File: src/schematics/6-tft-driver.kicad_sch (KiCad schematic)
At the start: 31 parts, among them Q601 NX6008NBKW, Q602 BC847BS, Q603 BC847BS, U601 TMUX1574RSV, U602 TMUX1574RSV, U603 TMUX1574RSV

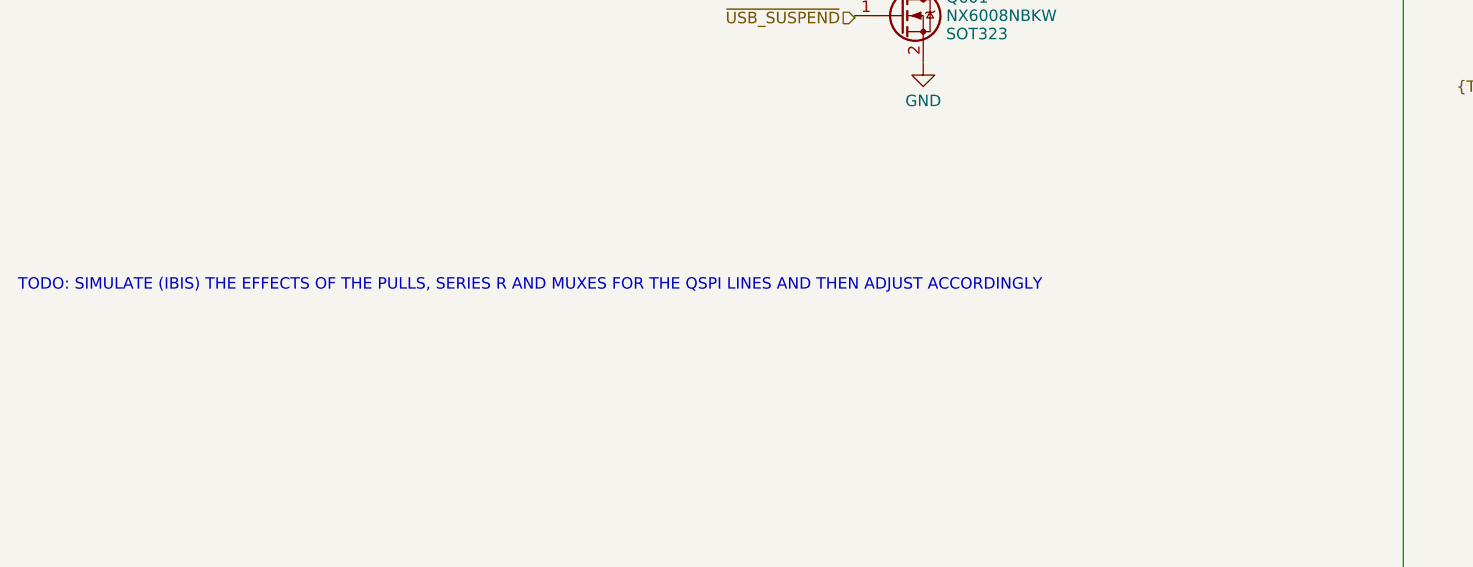
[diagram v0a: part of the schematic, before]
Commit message: Various tidy-ups and checks, mainly around the bypass capacitors.  Added a load of test points.
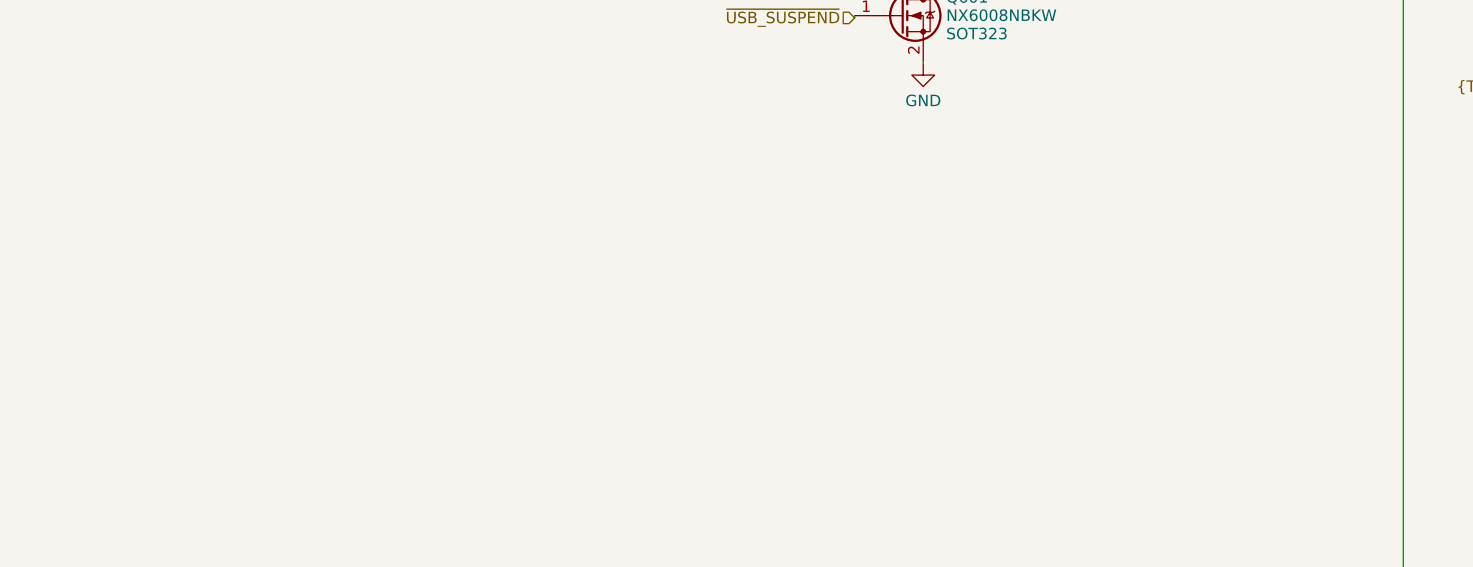
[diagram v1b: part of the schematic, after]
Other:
- note removed: "TODO: SIMULATE (IBIS) THE EFFECTS OF THE PULLS, SERIES R AND MUXES FOR THE QSPI LINES AND THEN ADJUST ACCORDINGLY"
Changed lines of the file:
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@@
     (stroke (width 0) (type default))
-  )
-  (text "TODO: SIMULATE (IBIS) THE EFFECTS OF THE PULLS, SERIES R AND MUXES FOR THE QSPI LINES AND THEN ADJUST ACCORDINGLY"
-    (at -39.624 88.9 0)
-    (effects (font (size 1.27 1.27)) (justify left bottom))
   )
   (text "Screen and Touch Resets" (at 48.26 132.334 0)

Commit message: Finalised various components and footprints.  Various tidy-ups.
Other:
- title: MSF Owl Clock - TFT Driver Module -> MSF Owl Clock - TFT Display Driver / Multiplexer Module
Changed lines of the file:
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@@
   (paper "A3")
   (title_block
-    (title "MSF Owl Clock - TFT Driver Module")
+    (title "MSF Owl Clock - TFT Display Driver / Multiplexer Module")
     (rev "0.1")
     (company "Pete Restall <pete@restall.net>")

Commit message: Added part numbers for the capacitors.
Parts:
- C601, C602, C603, C604, C605: ManufacturerPartNumber (none) -> CL05A475MP5NRNC
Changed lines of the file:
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@@
       (effects (font (size 1.27 1.27)) (justify left) hide)
     )
-    (property "ManufacturerPartNumber" "" (at 76.2 231.14 0)
+    (property "ManufacturerPartNumber" "CL05A475MP5NRNC" (at 76.2 231.14 0)
       (effects (font (size 1.27 1.27)) (justify left) hide)
     )
@@
       (effects (font (size 1.27 1.27)) (justify left) hide)
     )
-    (property "ManufacturerPartNumber" "" (at 193.04 35.56 0)
+    (property "ManufacturerPartNumber" "CL05A475MP5NRNC" (at 193.04 35.56 0)
       (effects (font (size 1.27 1.27)) (justify left) hide)
     )
@@
       (effects (font (size 1.27 1.27)) (justify left) hide)
     )
-    (property "ManufacturerPartNumber" "" (at 116.84 35.56 0)
+    (property "ManufacturerPartNumber" "CL05A475MP5NRNC" (at 116.84 35.56 0)
       (effects (font (size 1.27 1.27)) (justify left) hide)
     )
@@
       (effects (font (size 1.27 1.27)) (justify left) hide)
     )
-    (property "ManufacturerPartNumber" "" (at 269.24 35.56 0)
+    (property "ManufacturerPartNumber" "CL05A475MP5NRNC" (at 269.24 35.56 0)
       (effects (font (size 1.27 1.27)) (justify left) hide)
     )
@@
       (effects (font (size 1.27 1.27)) (justify left) hide)
     )
-    (property "ManufacturerPartNumber" "" (at 119.38 231.14 0)
-      (effects (font (size 1.27 1.27)) (justify left) hide)
-    )
+    (property "ManufacturerPartNumber" "CL05A475MP5NRNC" (at 119.38 231.14 0)
+      (effects (font (size 1.27 1.27)) (justify left) hide)
+    )

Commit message: Added part numbers for the resistors.
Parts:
- R601, R602, R603, R604, R605, R606, R607, R608, R609, R610, R611, R612, R613, R614, R615, R616, R617, R618: Manufacturer (none) -> Walsin; Manufacturer2 (none) -> Yageo; Manufacturer2PartNumber (none) -> RC0402FR-0733KL; ManufacturerPartNumber (none) -> WR04X3302FTL
- R619, R620: Manufacturer (none) -> Yageo; Manufacturer2 (none) -> Walsin; Manufacturer2PartNumber (none) -> WR04X18R0FTL; ManufacturerPartNumber (none) -> RC0402FR-0718RL

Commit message: Started to clean up the ERC flags.
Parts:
- added NT601, NT602, NT603, NT604: Net Tie, restall-generic-wires:net-tie-2-6mil, symbol restall-generic-wires:net-tie-2
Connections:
- net L_{TE}: now also NT603.1 (P1_PASSIVE), NT604.1 (P1_PASSIVE)
- net TFT_TP_INT0: now also NT601.2 (P2_PASSIVE)
- new net TFT_TEAR0: NT603.2 (P2_PASSIVE)
- new net TFT_TEAR1: NT604.2 (P2_PASSIVE)
- new net TFT_TP_INT1: NT602.2 (P2_PASSIVE)
- new net TP_INT: NT601.1 (P1_PASSIVE), NT602.1 (P1_PASSIVE)
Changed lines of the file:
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@@
     (stroke (width 0) (type default))
   )
-  (wire (pts (xy 218.44 241.3) (xy 259.08 241.3))
+  (wire (pts (xy 218.44 241.3) (xy 237.49 241.3))
     (stroke (width 0) (type default))
   )
@@
     (stroke (width 0) (type default))
   )
+  (wire (pts (xy 240.03 261.62) (xy 259.08 261.62))
+    (stroke (width 0) (type default))
+  )
   (wire (pts (xy 180.34 116.84) (xy 177.8 116.84))
     (stroke (width 0) (type default))
@@
     (stroke (width 0) (type default))
   )
-  (wire (pts (xy 218.44 236.22) (xy 259.08 236.22))
+  (wire (pts (xy 218.44 236.22) (xy 237.49 236.22))
     (stroke (width 0) (type default))
   )
@@
     (stroke (width 0) (type default))
   )
+  (wire (pts (xy 240.03 241.3) (xy 259.08 241.3))
+    (stroke (width 0) (type default))
+  )
   (wire (pts (xy 167.64 99.06) (xy 177.8 99.06))
     (stroke (width 0) (type default))
@@
     (stroke (width 0) (type default))
   )
+  (wire (pts (xy 240.03 236.22) (xy 259.08 236.22))
+    (stroke (width 0) (type default))
+  )
   (wire (pts (xy 175.26 139.7) (xy 175.26 142.24))
     (stroke (width 0) (type default))
@@
     (stroke (width 0) (type default))
   )
-  (wire (pts (xy 218.44 261.62) (xy 259.08 261.62))
+  (wire (pts (xy 218.44 261.62) (xy 237.49 261.62))
     (stroke (width 0) (type default))
   )
@@
     (stroke (width 0) (type default))
   )
+  (wire (pts (xy 240.03 256.54) (xy 259.08 256.54))
+    (stroke (width 0) (type default))
+  )
   (wire (pts (xy 320.04 99.06) (xy 320.04 93.98))
     (stroke (width 0) (type default))
@@
     (stroke (width 0) (type default))
   )
-  (wire (pts (xy 218.44 256.54) (xy 259.08 256.54))
+  (wire (pts (xy 218.44 256.54) (xy 237.49 256.54))
     (stroke (width 0) (type default))
   )
@@
     )
   )
+  (symbol (lib_id "restall-generic-wires:net-tie-2") (at 238.76 256.54 0) (unit 1)
+    (in_bom no) (on_board yes) (dnp no) (fields_autoplaced)
+    (property "Reference" "NT603" (at 238.76 254 0)
+      (effects (font (size 1.27 1.27)) hide)
+    )
+    (property "Value" "Net Tie" (at 238.76 259.08 0)
+      (effects (font (size 1.27 1.27)) hide)
+    )
+    (property "Footprint" "restall-generic-wires:net-tie-2-6mil" (at 238.76 261.112 0)
+      (effects (font (size 1.27 1.27)) hide)
+    )
+    (property "Datasheet" "~" (at 238.76 263.144 0)
+      (effects (font (size 1.27 1.27)) hide)
+    )
+    (pin "2")
+    (pin "1")
+    (instances
+      (project "msf-owl-clock"
+        (path "/56d623d3-22db-4d43-a9d9-e6bb4bb68946/2680f60f-7a4f-44d1-82ff-576d0b59662d"
+          (reference "NT603") (unit 1)
+        )
+      )
+    )
+  )
   (symbol (lib_id "restall-generic-capacitors:capacitor-unpolarised") (at 193.04 35.56 0) (unit 1)
     (in_bom yes) (on_board yes) (dnp no)
@@
         (path "/56d623d3-22db-4d43-a9d9-e6bb4bb68946/2680f60f-7a4f-44d1-82ff-576d0b59662d"
           (reference "R617") (unit 1)
+        )
+      )
+    )
+  )
+  (symbol (lib_id "restall-generic-wires:net-tie-2") (at 238.76 261.62 0) (unit 1)
+    (in_bom no) (on_board yes) (dnp no) (fields_autoplaced)
+    (property "Reference" "NT604" (at 238.76 259.08 0)
+      (effects (font (size 1.27 1.27)) hide)
+    )
+    (property "Value" "Net Tie" (at 238.76 264.16 0)
+      (effects (font (size 1.27 1.27)) hide)
+    )
+    (property "Footprint" "restall-generic-wires:net-tie-2-6mil" (at 238.76 266.192 0)
+      (effects (font (size 1.27 1.27)) hide)
+    )
+    (property "Datasheet" "~" (at 238.76 268.224 0)
+      (effects (font (size 1.27 1.27)) hide)
+    )
+    (pin "2")
+    (pin "1")
+    (instances
+      (project "msf-owl-clock"
+        (path "/56d623d3-22db-4d43-a9d9-e6bb4bb68946/2680f60f-7a4f-44d1-82ff-576d0b59662d"
+          (reference "NT604") (unit 1)
         )
       )
@@
     )
   )
+  (symbol (lib_id "restall-generic-wires:net-tie-2") (at 238.76 236.22 0) (unit 1)
+    (in_bom no) (on_board yes) (dnp no) (fields_autoplaced)
+    (property "Reference" "NT601" (at 238.76 233.68 0)
+      (effects (font (size 1.27 1.27)) hide)
+    )
+    (property "Value" "Net Tie" (at 238.76 238.76 0)
+      (effects (font (size 1.27 1.27)) hide)
+    )
+    (property "Footprint" "restall-generic-wires:net-tie-2-6mil" (at 238.76 240.792 0)
+      (effects (font (size 1.27 1.27)) hide)
+    )
+    (property "Datasheet" "~" (at 238.76 242.824 0)
+      (effects (font (size 1.27 1.27)) hide)
+    )
+    (pin "2")
+    (pin "1")
+    (instances
+      (project "msf-owl-clock"
+        (path "/56d623d3-22db-4d43-a9d9-e6bb4bb68946/2680f60f-7a4f-44d1-82ff-576d0b59662d"
+          (reference "NT601") (unit 1)
+        )
+      )
+    )
+  )
   (symbol (lib_id "restall-generic-power:GND") (at 184.15 116.84 0) (unit 1)
     (in_bom yes) (on_board yes) (dnp no) (fields_autoplaced)
@@
         )
       )
+    )
+  )
+  (symbol (lib_id "restall-generic-wires:net-tie-2") (at 238.76 241.3 0) (unit 1)
+    (in_bom no) (on_board yes) (dnp no) (fields_autoplaced)
+    (property "Reference" "NT602" (at 238.76 238.76 0)
+      (effects (font (size 1.27 1.27)) hide)
+    )
+    (property "Value" "Net Tie" (at 238.76 243.84 0)
+      (effects (font (size 1.27 1.27)) hide)
+    )
+    (property "Footprint" "restall-generic-wires:net-tie-2-6mil" (at 238.76 245.872 0)
+      (effects (font (size 1.27 1.27)) hide)
+    )
+    (property "Datasheet" "~" (at 238.76 247.904 0)
+      (effects (font (size 1.27 1.27)) hide)
+    )
+    (pin "2")
+    (pin "1")
+    (instances
+      (project "msf-owl-clock"
+        (path "/56d623d3-22db-4d43-a9d9-e6bb4bb68946/2680f60f-7a4f-44d1-82ff-576d0b59662d"
+          (reference "NT602") (unit 1)
+        )
+      )

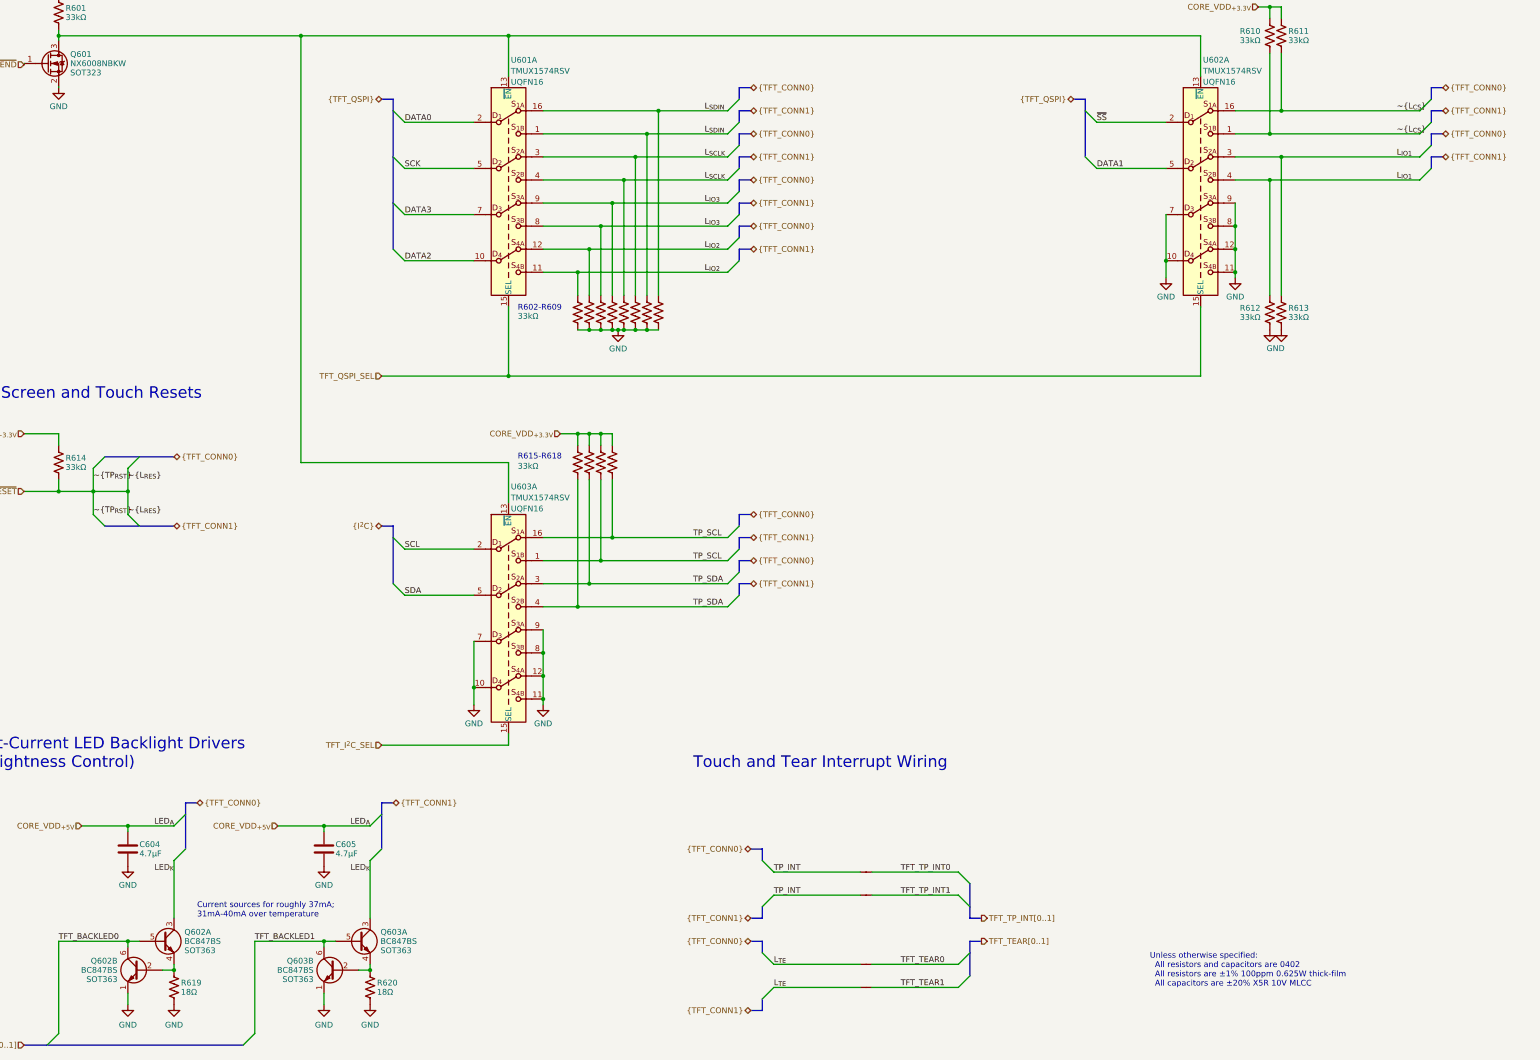
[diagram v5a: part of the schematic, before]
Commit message: Clean up the remaining ERC flags.
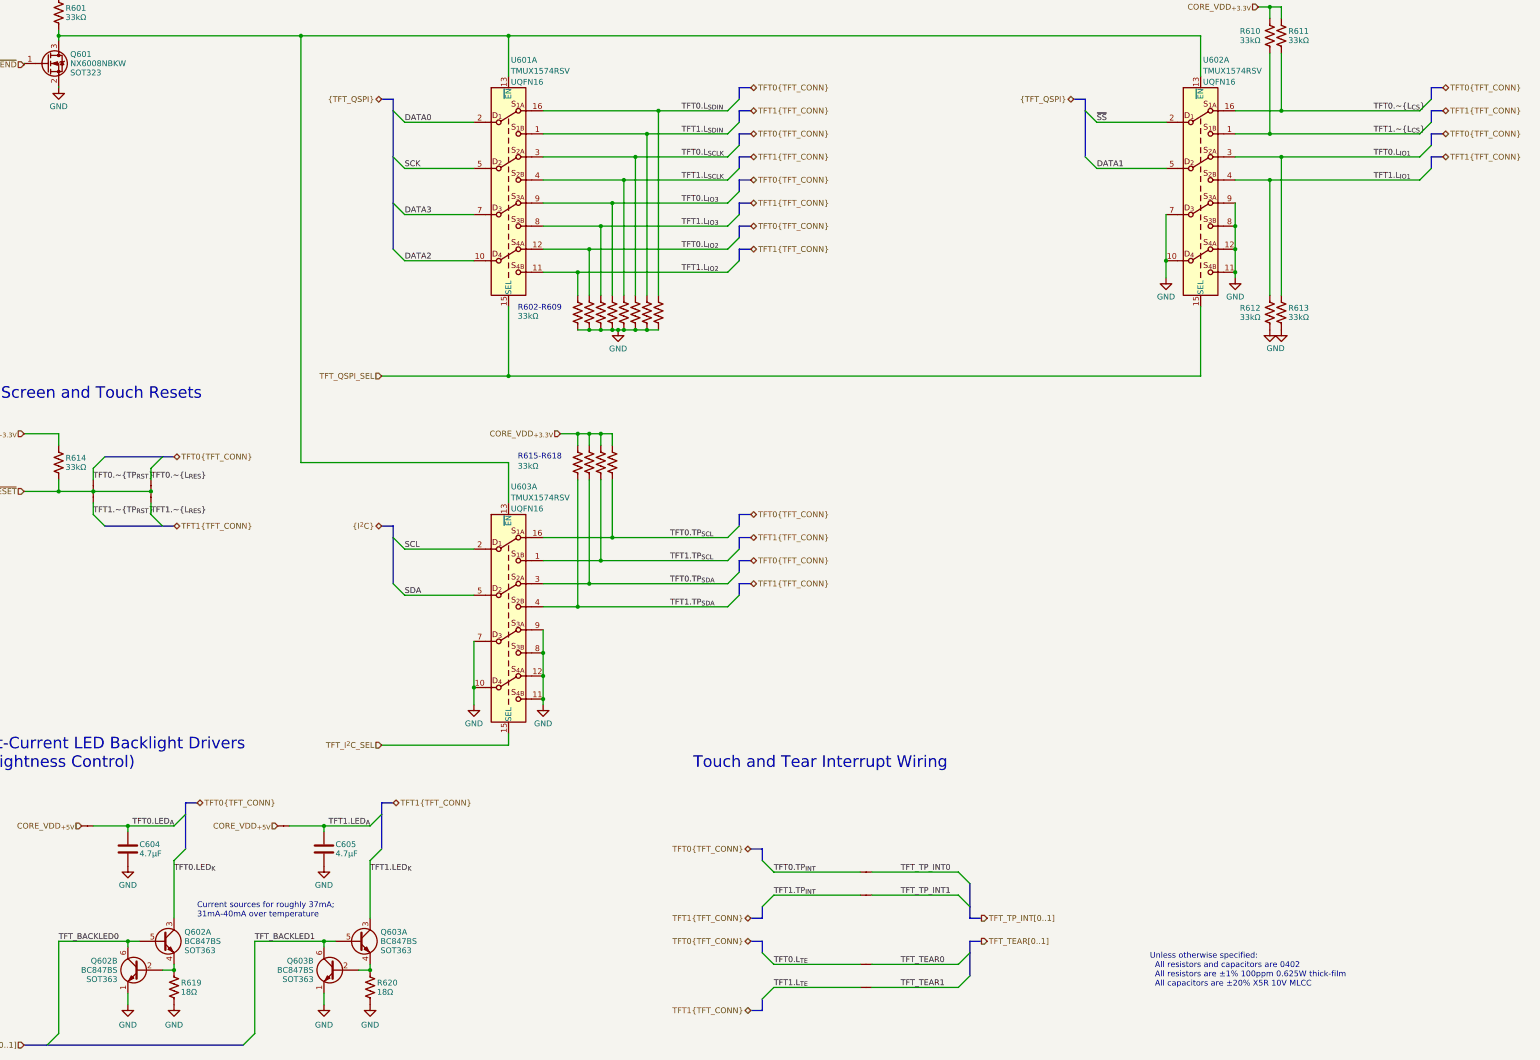
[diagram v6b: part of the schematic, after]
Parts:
- added NT605, NT606, NT607, NT608, NT609, NT610: Net Tie, restall-generic-wires:net-tie-2-6mil, symbol restall-generic-wires:net-tie-2
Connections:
- net CORE_VDD_{+5V}: now also NT609.1 (P1_PASSIVE), NT610.1 (P1_PASSIVE); no longer C604.1, C605.1
- net ~{TFT_RESET}: now also NT605.1 (P1_PASSIVE), NT606.1 (P1_PASSIVE), NT607.1 (P1_PASSIVE), NT608.1 (P1_PASSIVE)
- net GND renamed GND_PWRIN
- net LED_{K} renamed TFT0.LED_{K}
- net TFT0.LED_{K}: no longer Q603.3 (C)
- net L_{IO1} renamed TFT0.L_{IO1}
- net TFT0.L_{IO1}: no longer R612.1, U602.4
- net L_{IO2} renamed TFT0.L_{IO2}
- net TFT0.L_{IO2}: no longer R602.1, U601.11
- net L_{IO3} renamed TFT0.L_{IO3}
- net TFT0.L_{IO3}: no longer R604.1, U601.8
- net L_{SCLK} renamed TFT0.L_{SCLK}
- net TFT0.L_{SCLK}: no longer R606.1, U601.4
- net L_{SDIN} renamed TFT0.L_{SDIN}
- net TFT0.L_{SDIN}: no longer R608.1, U601.1
- net L_{TE} renamed TFT0.L_{TE}
- net TFT0.L_{TE}: no longer NT604.1 (P1_PASSIVE)
- net TP_INT renamed TFT0.TP_{INT}
- net TFT0.TP_{INT}: no longer NT602.1 (P1_PASSIVE)
- net TP_SCL renamed TFT0.TP_{SCL}
- net TFT0.TP_{SCL}: no longer R617.2, U603.1
- net TP_SDA renamed TFT0.TP_{SDA}
- net TFT0.TP_{SDA}: no longer R615.2, U603.4
- net ~{L_{CS}} renamed TFT0.~{L_{CS}}
- net TFT0.~{L_{CS}}: no longer R610.2, U602.1
- new net TFT0.LED_{A}: C604.1, NT609.2 (P2_PASSIVE)
- new net TFT0.~{L_{RES}}: NT607.2 (P2_PASSIVE)
- new net TFT0.~{TP_{RST}}: NT605.2 (P2_PASSIVE)
- new net TFT1.LED_{A}: C605.1, NT610.2 (P2_PASSIVE)
- new net TFT1.LED_{K}: Q603.3 (C)
- new net TFT1.L_{IO1}: R612.1, U602.4
- new net TFT1.L_{IO2}: R602.1, U601.11
- new net TFT1.L_{IO3}: R604.1, U601.8
- new net TFT1.L_{SCLK}: R606.1, U601.4
- new net TFT1.L_{SDIN}: R608.1, U601.1
- new net TFT1.L_{TE}: NT604.1 (P1_PASSIVE)
- new net TFT1.TP_{INT}: NT602.1 (P1_PASSIVE)
- new net TFT1.TP_{SCL}: R617.2, U603.1
- new net TFT1.TP_{SDA}: R615.2, U603.4
- new net TFT1.~{L_{CS}}: R610.2, U602.1
- new net TFT1.~{L_{RES}}: NT608.2 (P2_PASSIVE)
- new net TFT1.~{TP_{RST}}: NT606.2 (P2_PASSIVE)

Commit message: Started to lay out the PCB.
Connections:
- net GND_PWRIN renamed GND

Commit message: PCB routing.
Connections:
- net DATA0: now also U601.7; no longer U601.2
- net DATA1: now also U601.5; no longer U602.5
- net DATA3: now also U601.2; no longer U601.7
- net GND: now also U602.3, U602.4, U602.5; no longer U602.7, U602.8, U602.9
- net SCK: now also U602.7; no longer U601.5
- net TFT0.L_{IO1}: now also R607.1, U601.3; no longer R613.1, U602.3
- net TFT0.L_{IO3}: now also R609.1, U601.16; no longer R605.1, U601.9
- net TFT0.L_{SCLK}: now also R613.1, U602.9; no longer R607.1, U601.3
- net TFT0.L_{SDIN}: now also R605.1, U601.9; no longer R609.1, U601.16
- net TFT1.L_{IO1}: now also R606.1, U601.4; no longer R612.1, U602.4
- net TFT1.L_{IO3}: now also R608.1, U601.1; no longer R604.1, U601.8
- net TFT1.L_{SCLK}: now also R612.1, U602.8; no longer R606.1, U601.4
- net TFT1.L_{SDIN}: now also R604.1, U601.8; no longer R608.1, U601.1
